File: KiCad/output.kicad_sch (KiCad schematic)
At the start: 1 part

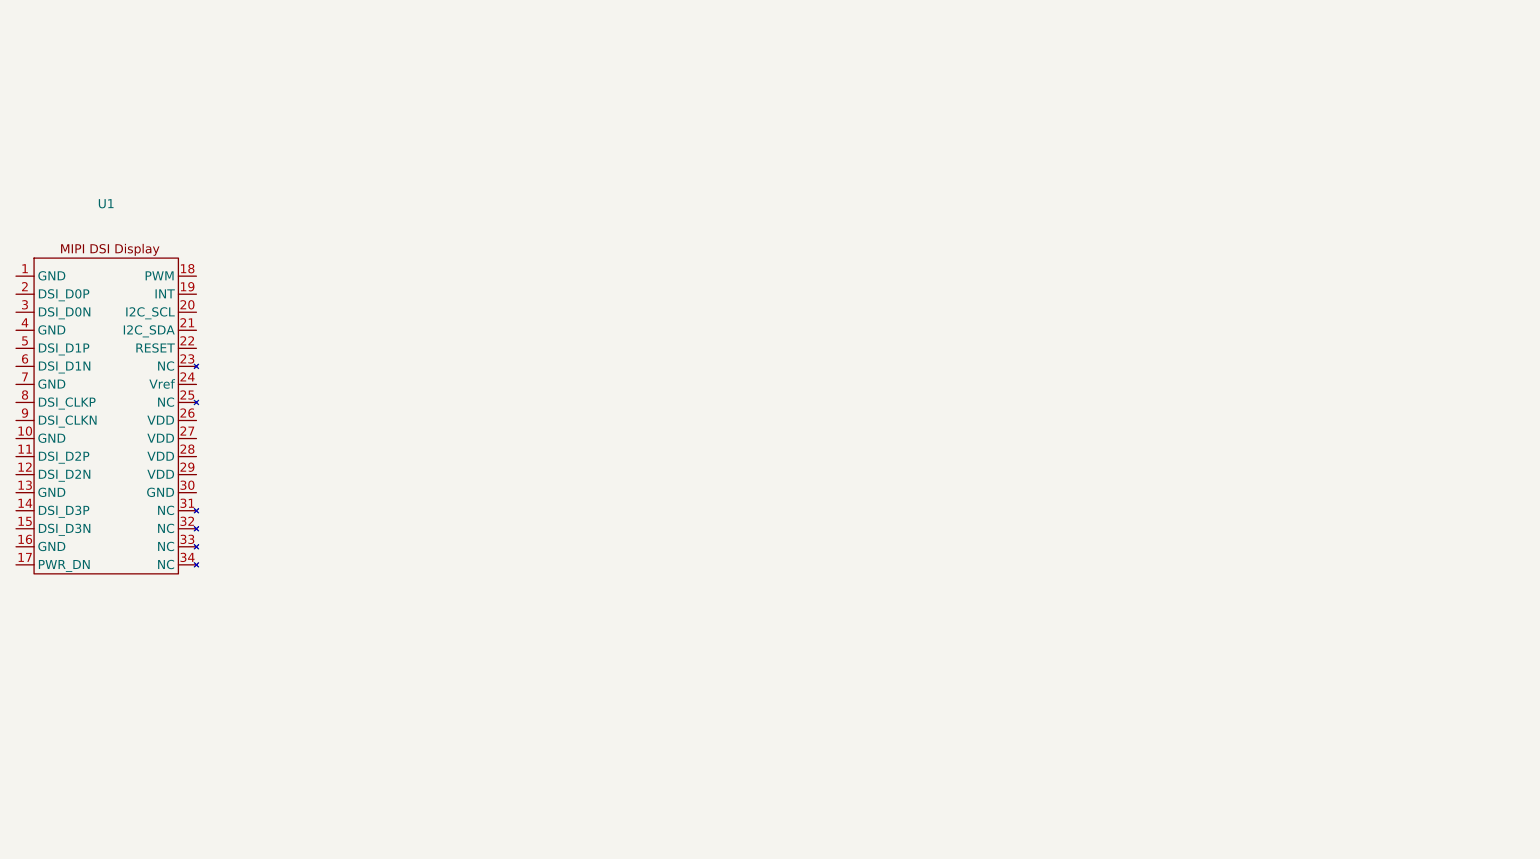
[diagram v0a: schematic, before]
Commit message: redid button pull up. Added initial joystick and display symbols
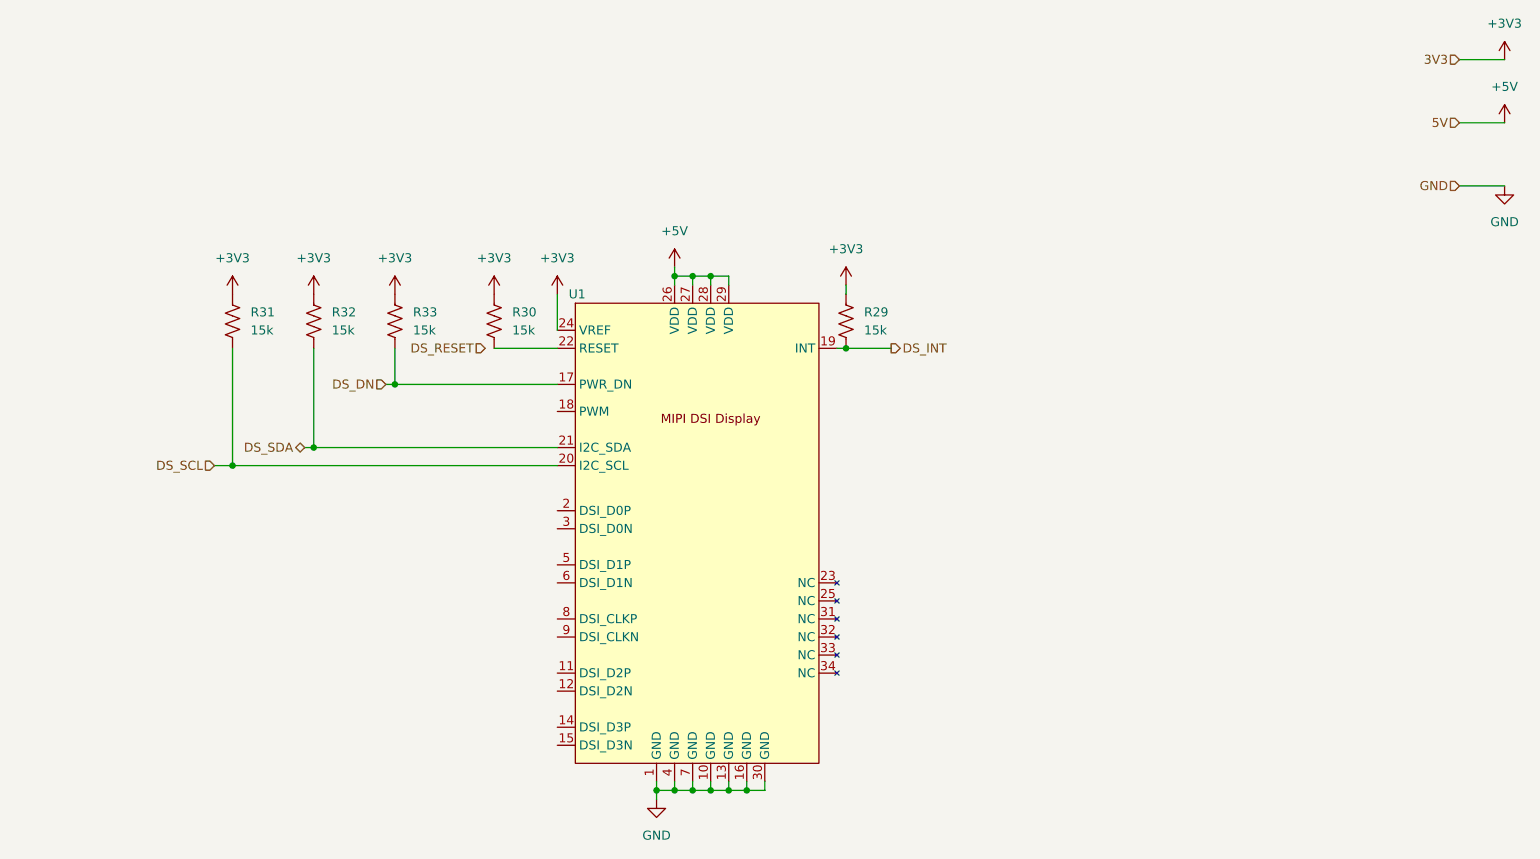
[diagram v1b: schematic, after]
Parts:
- added R29, R30, R31, R32, R33: 15k, symbol Device:R_US
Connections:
- net GND: now reaches U1.1 (GND)
- net GND: now also U1.10 (GND), U1.13 (GND), U1.16 (GND), U1.30 (GND), U1.4 (GND), U1.7 (GND)
- net DS_DN: now reaches U1.17 (PWR_DN)
- net DS_DN: now also R33.2
- net DS_INT: now reaches U1.19 (INT)
- net DS_INT: now also R29.2
- net DS_SCL: now reaches U1.20 (I2C_SCL)
- net DS_SCL: now also R31.2
- net DS_SDA: now reaches U1.21 (I2C_SDA)
- net DS_SDA: now also R32.2
- net at U1.22 (RESET): now also R30.2
- net +3V3: now reaches U1.24 (VREF)
- net +3V3: now also R29.1, R30.1, R31.1, R32.1, R33.1
- net +5V: now reaches U1.26 (VDD)
- net +5V: now also U1.27 (VDD), U1.28 (VDD), U1.29 (VDD)
